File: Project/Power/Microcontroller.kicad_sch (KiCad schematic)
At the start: 12 parts, among them J5 SWD, SW1 SW_Push, U14 MIC5219-3.3YM5, U15 STM32L422KBTx

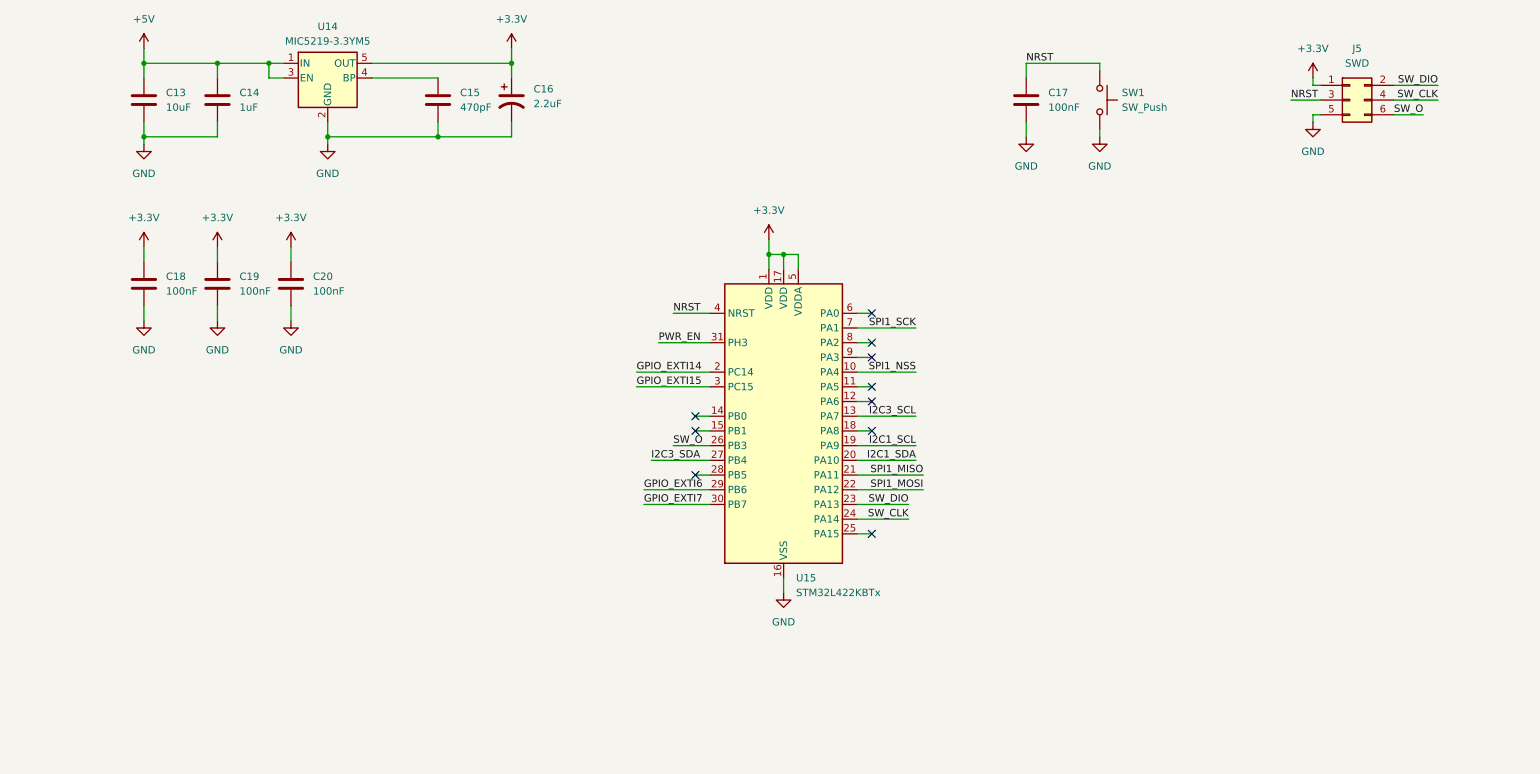
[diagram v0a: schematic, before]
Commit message: Make microcontroller always-on
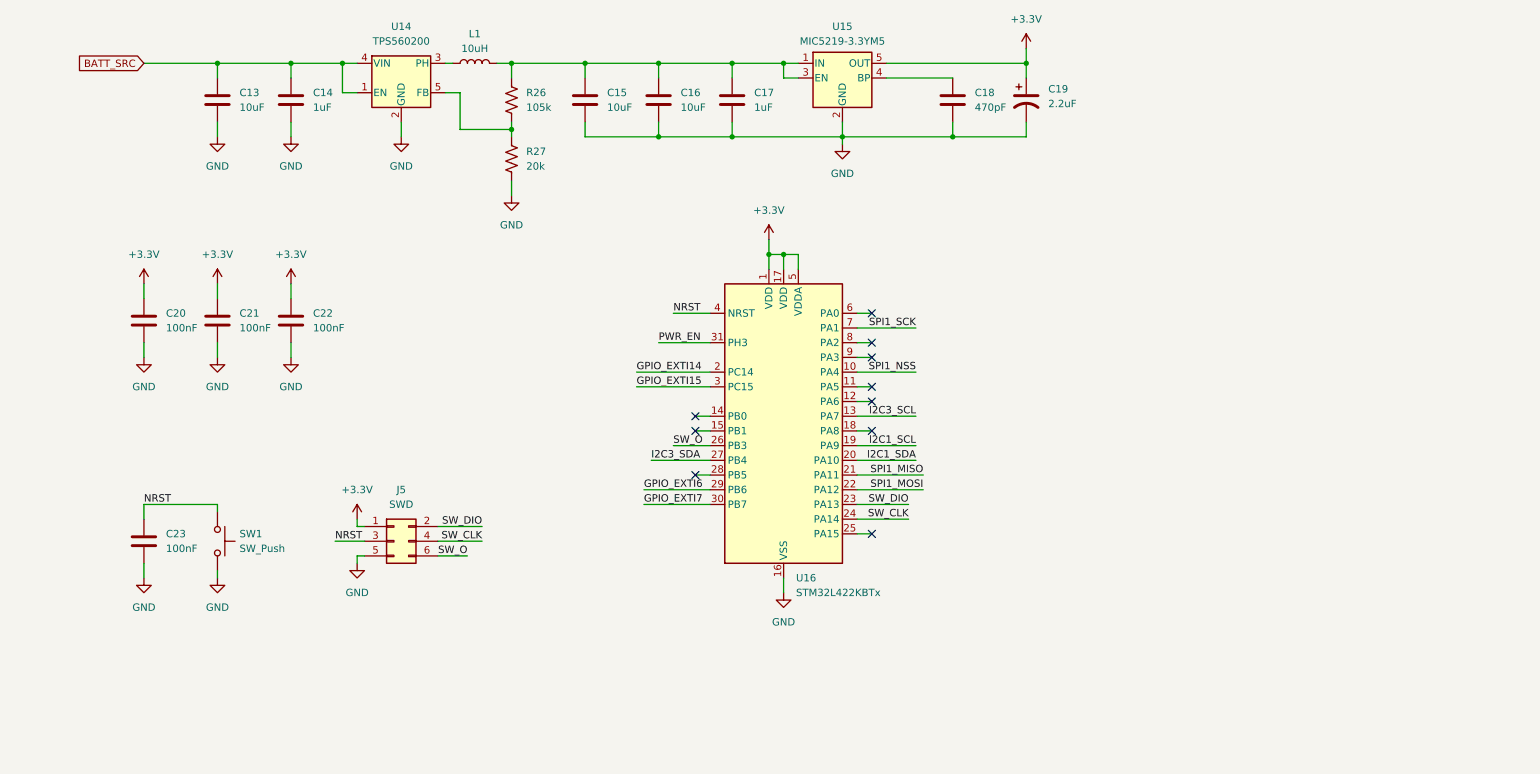
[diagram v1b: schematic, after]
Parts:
- added C15, C16: 10uF, Capacitor_SMD:C_1206_3216Metric, symbol Device:C
- added C17: 1uF, Capacitor_SMD:C_0603_1608Metric, symbol Device:C
- added L1: 10uH, Inductor_SMD:L_1210_3225Metric, symbol Device:L
- added R26: 105k, Resistor_SMD:R_0603_1608Metric, symbol Device:R_US
- added R27: 20k, Resistor_SMD:R_0603_1608Metric, symbol Device:R_US
- added U14: TPS560200, Package_TO_SOT_SMD:SOT-23-5, symbol Regulator_Switching:TPS560200
- renumbered C15 to C18, C16 to C19, C18 to C20, C19 to C21, C20 to C22, C17 to C23, U14 to U15, U15 to U16
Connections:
- net GND: now also C15.2, C16.2, C17.2, R27.2, U14.2 (GND)
- net +5V: no longer names the net of U15.1 (IN), U15.3 (EN)
- net +5V: now also C15.1, C16.1, C17.1, L1.2, R26.1; no longer C13.1, C14.1
- new net: R26.2, R27.1, U14.5 (FB)
- new net: L1.1, U14.3 (PH)
- new net BATT_SRC: C13.1, C14.1, U14.1 (EN), U14.4 (VIN)
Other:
- moved on the sheet: C13, C14, C18, C19, C20, C21, C22, C23, J5, SW1, U15

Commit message: Connect microcontroller to main enable switch
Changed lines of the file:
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@@
 	(title_block
 		(title "Microcontroller")
-		(date "2026-03-11")
+		(date "2026-03-12")
 		(rev "B")
 		(company "CU Boulder Senior Design Team 29 - Xu Lab")
@@
 	(wire
 		(pts
+			(xy 76.2 152.4) (xy 88.9 152.4)
+		)
+		(stroke
+			(width 0)
+			(type default)
+		)
+	)
+	(wire
+		(pts
 			(xy 63.5 78.74) (xy 63.5 76.2)
 		)
@@
 	(label "GPIO_EXTI15"
 		(at 123.19 93.98 0)
+		(effects
+			(font
+				(size 1.27 1.27)
+			)
+			(justify left bottom)
+		)
+	)
+	(label "PWR_EN"
+		(at 76.2 152.4 0)
 		(effects
 			(font
@@
 		)
 	)
+	(hierarchical_label "PWR_EN"
+		(shape output)
+		(at 88.9 152.4 0)
+		(effects
+			(font
+				(size 1.27 1.27)
+			)
+			(justify left)
+		)
+	)

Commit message: Add SPI and I2C connectors for microcontroller
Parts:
- added C23, C25: 100nF, Capacitor_SMD:C_0603_1608Metric, symbol Device:C
- added J5: I2C, Connector_JST:JST_GH_SM04B-GHS-TB_1x04-1MP_P1.25mm_Horizontal, symbol Connector_Generic:Conn_01x04
- added J6: SPI1, Connector_JST:JST_GH_SM06B-GHS-TB_1x06-1MP_P1.25mm_Horizontal, symbol Connector_Generic:Conn_01x06
- renumbered C23 to C24, J5 to J7
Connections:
- net +3.3V: now also C23.1, C25.1, J5.1 (Pin_1), J6.1 (Pin_1)
- net GND: now also C23.2, C25.2, J5.4 (Pin_4), J6.6 (Pin_6)
- net I2C1_SCL: now also J5.2 (Pin_2)
- net I2C1_SDA: now also J5.3 (Pin_3)
- net SPI1_MISO: now also J6.4 (Pin_4)
- net SPI1_MOSI: now also J6.3 (Pin_3)
- net SPI1_NSS: now also J6.5 (Pin_5)
- net SPI1_SCK: now also J6.2 (Pin_2)

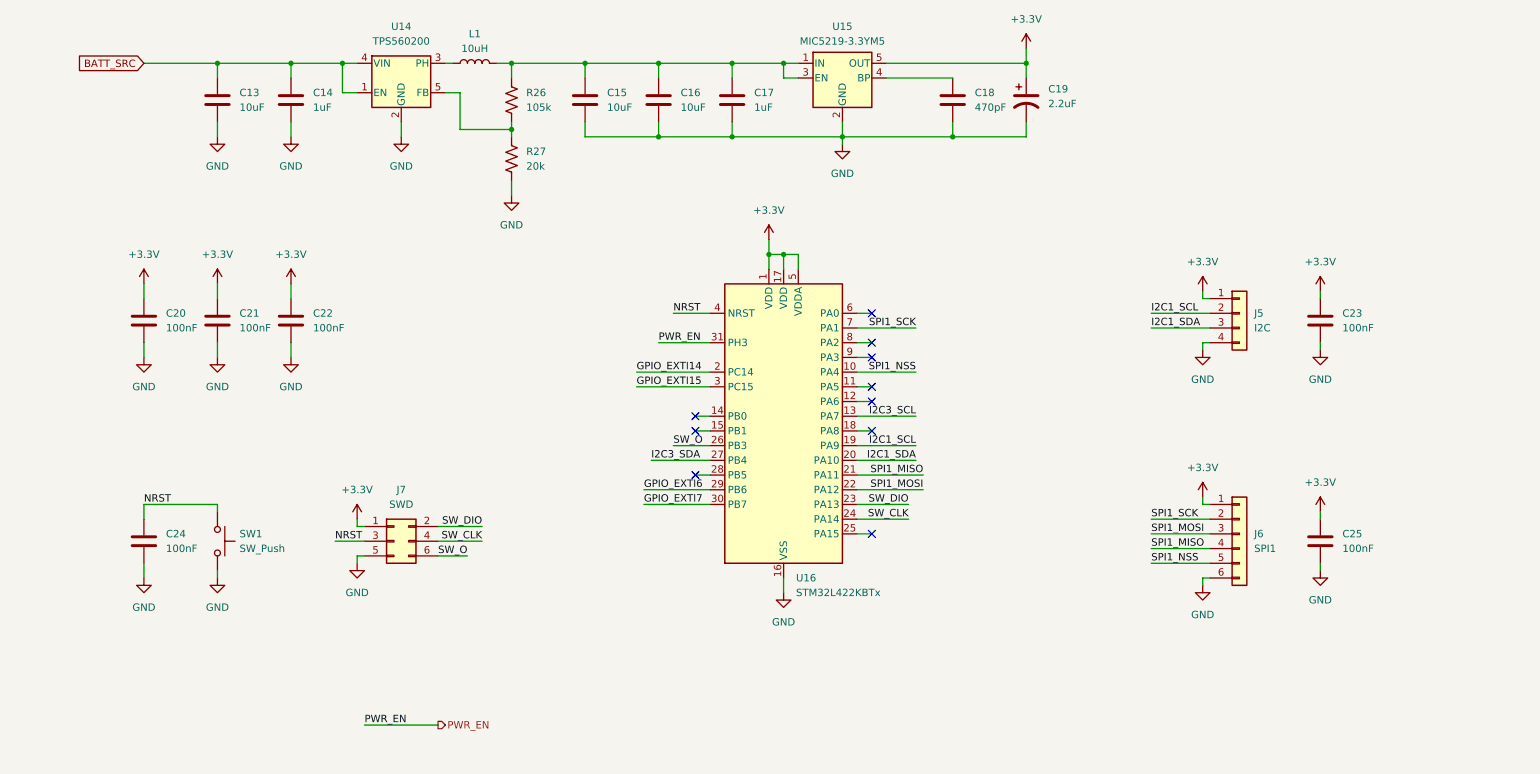
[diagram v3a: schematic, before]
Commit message: Reorganize converters
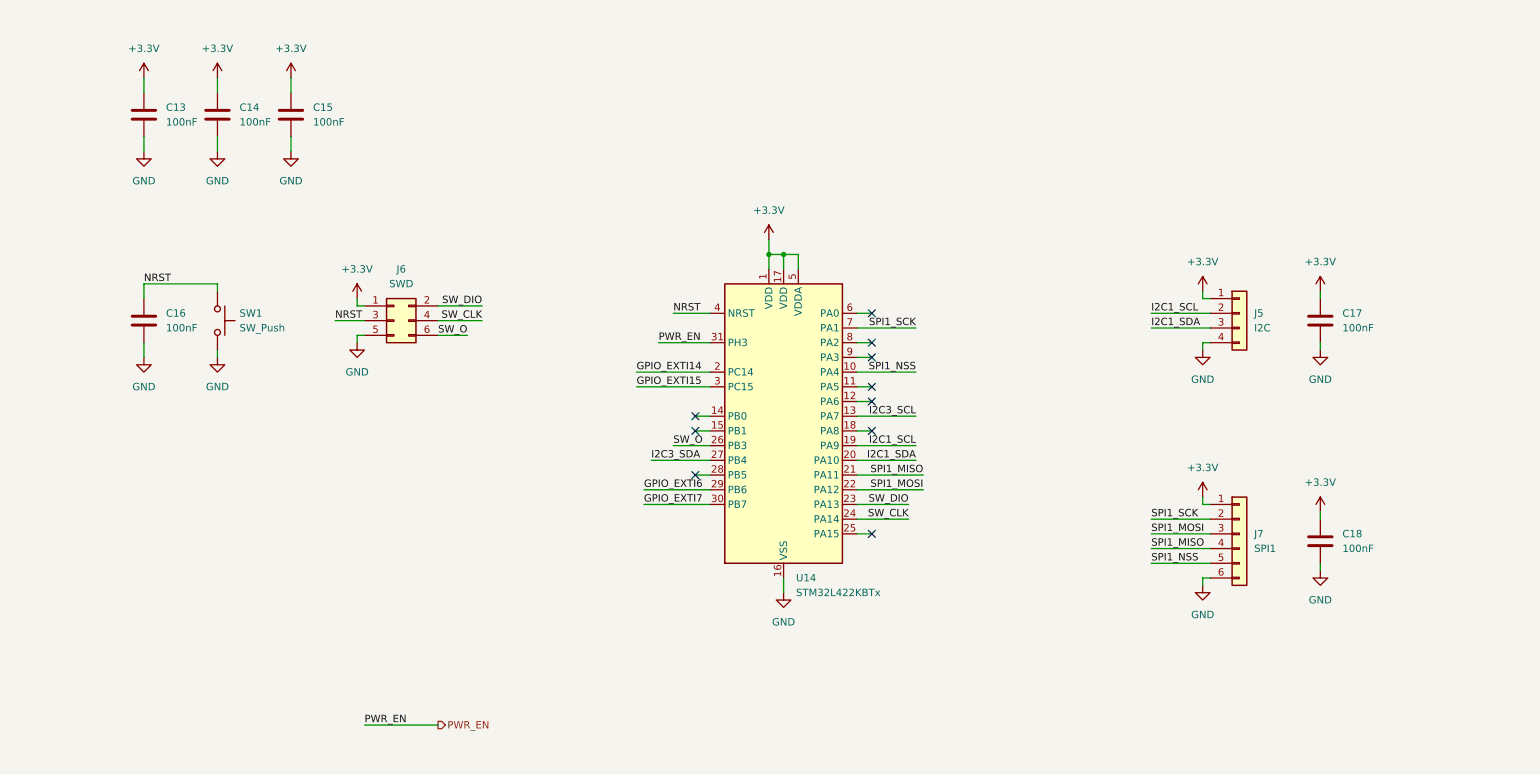
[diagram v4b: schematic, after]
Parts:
- removed C13, C15, C16: 10uF, Capacitor_SMD:C_1206_3216Metric, symbol Device:C
- removed C14, C17: 1uF, Capacitor_SMD:C_0603_1608Metric, symbol Device:C
- removed C18: 470pF, Capacitor_SMD:C_0603_1608Metric, symbol Device:C
- removed C19: 2.2uF, Capacitor_Tantalum_SMD:CP_EIA-3216-18_Kemet-A, symbol Device:C_Polarized_US
- removed L1: 10uH, Inductor_SMD:L_1210_3225Metric, symbol Device:L
- removed R26: 105k, Resistor_SMD:R_0603_1608Metric, symbol Device:R_US
- removed R27: 20k, Resistor_SMD:R_0603_1608Metric, symbol Device:R_US
- removed U14: TPS560200, Package_TO_SOT_SMD:SOT-23-5, symbol Regulator_Switching:TPS560200
- removed U15: MIC5219-3.3YM5, Package_TO_SOT_SMD:SOT-23-5, symbol Regulator_Linear:MIC5219-3.3YM5
- renumbered C20 to C13, C21 to C14, C22 to C15, C24 to C16, C23 to C17, C25 to C18, J7 to J6, J6 to J7, U16 to U14
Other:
- moved on the sheet: C13, C14, C15, C16, J6, SW1

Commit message: Add servo connectors
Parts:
- renumbered J5 to J13, J6 to J14, J7 to J15
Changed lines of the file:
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@@
 		(dnp no)
 		(fields_autoplaced yes)
-		(property "Reference" "#PWR062"
+		(property "Reference" "#PWR078"
 			(at 63.5 44.45 0)
 			(effects
@@
 			(project "XuLabPower"
 				(path "/71bb14ae-b730-4d22-a41d-cf68989dae2d/2597d1dc-5599-49ba-bd43-a24c9bb27c8e"
-					(reference "#PWR062")
+					(reference "#PWR078")
 					(unit 1)
 				)
@@
 		(dnp no)
 		(fields_autoplaced yes)
-		(property "Reference" "J7"
+		(property "Reference" "J15"
 			(at 229.87 119.3799 0)
 			(effects
@@
 			(project "XuLabPower"
 				(path "/71bb14ae-b730-4d22-a41d-cf68989dae2d/2597d1dc-5599-49ba-bd43-a24c9bb27c8e"
-					(reference "J7")
+					(reference "J15")
 					(unit 1)
 				)
@@
 		(dnp no)
 		(fields_autoplaced yes)
-		(property "Reference" "#PWR065"
+		(property "Reference" "#PWR081"
 			(at 63.5 59.69 0)
 			(effects
@@
 			(project "XuLabPower"
 				(path "/71bb14ae-b730-4d22-a41d-cf68989dae2d/2597d1dc-5599-49ba-bd43-a24c9bb27c8e"
-					(reference "#PWR065")
+					(reference "#PWR081")
 					(unit 1)
 				)
@@
 		(dnp no)
 		(fields_autoplaced yes)
-		(property "Reference" "#PWR067"
+		(property "Reference" "#PWR083"
 			(at 220.98 81.28 0)
 			(effects
@@
 			(project "XuLabPower"
 				(path "/71bb14ae-b730-4d22-a41d-cf68989dae2d/2597d1dc-5599-49ba-bd43-a24c9bb27c8e"
-					(reference "#PWR067")
+					(reference "#PWR083")
 					(unit 1)
 				)
@@
 		(dnp no)
 		(fields_autoplaced yes)
-		(property "Reference" "#PWR074"
+		(property "Reference" "#PWR090"
 			(at 50.8 95.25 0)
 			(effects
@@
 			(project "XuLabPower"
 				(path "/71bb14ae-b730-4d22-a41d-cf68989dae2d/2597d1dc-5599-49ba-bd43-a24c9bb27c8e"
-					(reference "#PWR074")
+					(reference "#PWR090")
 					(unit 1)
 				)
@@
 		(dnp no)
 		(fields_autoplaced yes)
-		(property "Reference" "#PWR066"
+		(property "Reference" "#PWR082"
 			(at 146.05 72.39 0)
 			(effects
@@
 			(project "XuLabPower"
 				(path "/71bb14ae-b730-4d22-a41d-cf68989dae2d/2597d1dc-5599-49ba-bd43-a24c9bb27c8e"
-					(reference "#PWR066")
+					(reference "#PWR082")
 					(unit 1)
 				)
@@
 		(dnp no)
 		(fields_autoplaced yes)
-		(property "Reference" "#PWR060"
+		(property "Reference" "#PWR076"
 			(at 38.1 44.45 0)
 			(effects
@@
 			(project "XuLabPower"
 				(path "/71bb14ae-b730-4d22-a41d-cf68989dae2d/2597d1dc-5599-49ba-bd43-a24c9bb27c8e"
-					(reference "#PWR060")
+					(reference "#PWR076")
 					(unit 1)
 				)
@@
 		(dnp no)
 		(fields_autoplaced yes)
-		(property "Reference" "#PWR070"
+		(property "Reference" "#PWR086"
 			(at 74.93 92.71 0)
 			(effects
@@
 			(project "XuLabPower"
 				(path "/71bb14ae-b730-4d22-a41d-cf68989dae2d/2597d1dc-5599-49ba-bd43-a24c9bb27c8e"
-					(reference "#PWR070")
+					(reference "#PWR086")
 					(unit 1)
 				)
@@
 		(dnp no)
 		(fields_autoplaced yes)
-		(property "Reference" "#PWR079"
+		(property "Reference" "#PWR095"
 			(at 148.59 135.89 0)
 			(effects
@@
 			(project "XuLabPower"
 				(path "/71bb14ae-b730-4d22-a41d-cf68989dae2d/2597d1dc-5599-49ba-bd43-a24c9bb27c8e"
-					(reference "#PWR079")
+					(reference "#PWR095")
 					(unit 1)
 				)
@@
 		(dnp no)
 		(fields_autoplaced yes)
-		(property "Reference" "#PWR064"
+		(property "Reference" "#PWR080"
 			(at 50.8 59.69 0)
 			(effects
@@
 			(project "XuLabPower"
 				(path "/71bb14ae-b730-4d22-a41d-cf68989dae2d/2597d1dc-5599-49ba-bd43-a24c9bb27c8e"
-					(reference "#PWR064")
+					(reference "#PWR080")
 					(unit 1)
 				)
@@
 		(dnp no)
 		(fields_autoplaced yes)
-		(property "Reference" "J5"
+		(property "Reference" "J13"
 			(at 229.87 81.2799 0)
 			(effects
@@
 			(project "XuLabPower"
 				(path "/71bb14ae-b730-4d22-a41d-cf68989dae2d/2597d1dc-5599-49ba-bd43-a24c9bb27c8e"
-					(reference "J5")
+					(reference "J13")
 					(unit 1)
 				)
@@
 		(dnp no)
 		(fields_autoplaced yes)
-		(property "Reference" "#PWR068"
+		(property "Reference" "#PWR084"
 			(at 241.3 81.28 0)
 			(effects
@@
 			(project "XuLabPower"
 				(path "/71bb14ae-b730-4d22-a41d-cf68989dae2d/2597d1dc-5599-49ba-bd43-a24c9bb27c8e"
-					(reference "#PWR068")
+					(reference "#PWR084")
 					(unit 1)
 				)
@@
 		(dnp no)
 		(fields_autoplaced yes)
-		(property "Reference" "#PWR061"
+		(property "Reference" "#PWR077"
 			(at 50.8 44.45 0)
 			(effects
@@
 			(project "XuLabPower"
 				(path "/71bb14ae-b730-4d22-a41d-cf68989dae2d/2597d1dc-5599-49ba-bd43-a24c9bb27c8e"
-					(reference "#PWR061")
+					(reference "#PWR077")
 					(unit 1)
 				)
@@
 		(dnp no)
 		(fields_autoplaced yes)
-		(property "Reference" "#PWR071"
+		(property "Reference" "#PWR087"
 			(at 220.98 93.98 0)
 			(effects
@@
 			(project "XuLabPower"
 				(path "/71bb14ae-b730-4d22-a41d-cf68989dae2d/2597d1dc-5599-49ba-bd43-a24c9bb27c8e"
-					(reference "#PWR071")
+					(reference "#PWR087")
 					(unit 1)
 				)
@@
 		(dnp no)
 		(fields_autoplaced yes)
-		(property "Reference" "#PWR077"
+		(property "Reference" "#PWR093"
 			(at 241.3 132.08 0)
 			(effects
@@
 			(project "XuLabPower"
 				(path "/71bb14ae-b730-4d22-a41d-cf68989dae2d/2597d1dc-5599-49ba-bd43-a24c9bb27c8e"
-					(reference "#PWR077")
+					(reference "#PWR093")
 					(unit 1)
 				)
@@
 		(dnp no)
 		(fields_autoplaced yes)
-		(property "Reference" "#PWR069"
+		(property "Reference" "#PWR085"
 			(at 74.93 82.55 0)
 			(effects
@@
 			(project "XuLabPower"
 				(path "/71bb14ae-b730-4d22-a41d-cf68989dae2d/2597d1dc-5599-49ba-bd43-a24c9bb27c8e"
-					(reference "#PWR069")
+					(reference "#PWR085")
 					(unit 1)
 				)
@@
 		(dnp no)
 		(fields_autoplaced yes)
-		(property "Reference" "#PWR063"
+		(property "Reference" "#PWR079"
 			(at 38.1 59.69 0)
 			(effects
@@
 			(project "XuLabPower"
 				(path "/71bb14ae-b730-4d22-a41d-cf68989dae2d/2597d1dc-5599-49ba-bd43-a24c9bb27c8e"
-					(reference "#PWR063")
+					(reference "#PWR079")
 					(unit 1)
 				)
@@
 		(dnp no)
 		(fields_autoplaced yes)
-		(property "Reference" "#PWR078"
+		(property "Reference" "#PWR094"
 			(at 220.98 134.62 0)
 			(effects
@@
 			(project "XuLabPower"
 				(path "/71bb14ae-b730-4d22-a41d-cf68989dae2d/2597d1dc-5599-49ba-bd43-a24c9bb27c8e"
-					(reference "#PWR078")
+					(reference "#PWR094")
 					(unit 1)
 				)
@@
 		(dnp no)
 		(fields_autoplaced yes)
-		(property "Reference" "J6"
+		(property "Reference" "J14"
 			(at 82.55 73.66 0)
 			(effects
@@
 			(project "XuLabPower"
 				(path "/71bb14ae-b730-4d22-a41d-cf68989dae2d/2597d1dc-5599-49ba-bd43-a24c9bb27c8e"
-					(reference "J6")
+					(reference "J14")
 					(unit 1)
 				)
@@
 		(dnp no)
 		(fields_autoplaced yes)
-		(property "Reference" "#PWR076"
+		(property "Reference" "#PWR092"
 			(at 241.3 119.38 0)
 			(effects
@@
 			(project "XuLabPower"
 				(path "/71bb14ae-b730-4d22-a41d-cf68989dae2d/2597d1dc-5599-49ba-bd43-a24c9bb27c8e"
-					(reference "#PWR076")
+					(reference "#PWR092")
 					(unit 1)
 				)
@@
 		(dnp no)
 		(fields_autoplaced yes)
-		(property "Reference" "#PWR073"
+		(property "Reference" "#PWR089"
 			(at 38.1 95.25 0)
 			(effects
@@
 			(project "XuLabPower"
 				(path "/71bb14ae-b730-4d22-a41d-cf68989dae2d/2597d1dc-5599-49ba-bd43-a24c9bb27c8e"
-					(reference "#PWR073")
+					(reference "#PWR089")
 					(unit 1)
 				)
@@
 		(dnp no)
 		(fields_autoplaced yes)
-		(property "Reference" "#PWR072"
+		(property "Reference" "#PWR088"
 			(at 241.3 93.98 0)
 			(effects
@@
 			(project "XuLabPower"
 				(path "/71bb14ae-b730-4d22-a41d-cf68989dae2d/2597d1dc-5599-49ba-bd43-a24c9bb27c8e"
-					(reference "#PWR072")
+					(reference "#PWR088")
 					(unit 1)
 				)
@@
 		(dnp no)
 		(fields_autoplaced yes)
-		(property "Reference" "#PWR075"
+		(property "Reference" "#PWR091"
 			(at 220.98 116.84 0)
 			(effects
@@
 			(project "XuLabPower"
 				(path "/71bb14ae-b730-4d22-a41d-cf68989dae2d/2597d1dc-5599-49ba-bd43-a24c9bb27c8e"
-					(reference "#PWR075")
-					(unit 1)
-				)
+					(reference "#PWR091")
+					(unit 1)
+				)
